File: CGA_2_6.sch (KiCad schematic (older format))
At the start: 16 parts, among them U10 74153, U101 74S174, U24 74LS244, U31 74S08, U32 74LS166, U33 MK36000, U34 74LS273, U35 74LS273, U36 74LS244, U37 74LS374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

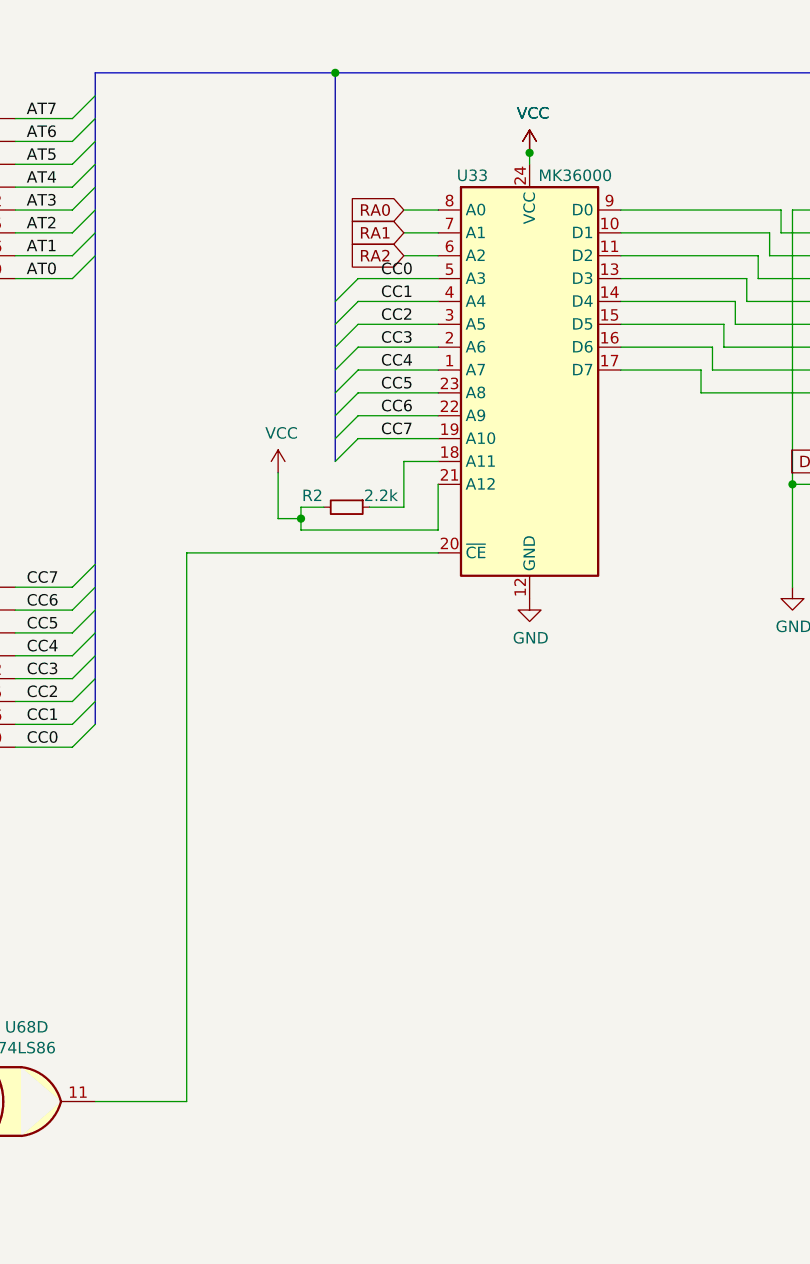
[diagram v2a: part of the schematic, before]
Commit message: Replace MK36000 with 27C256
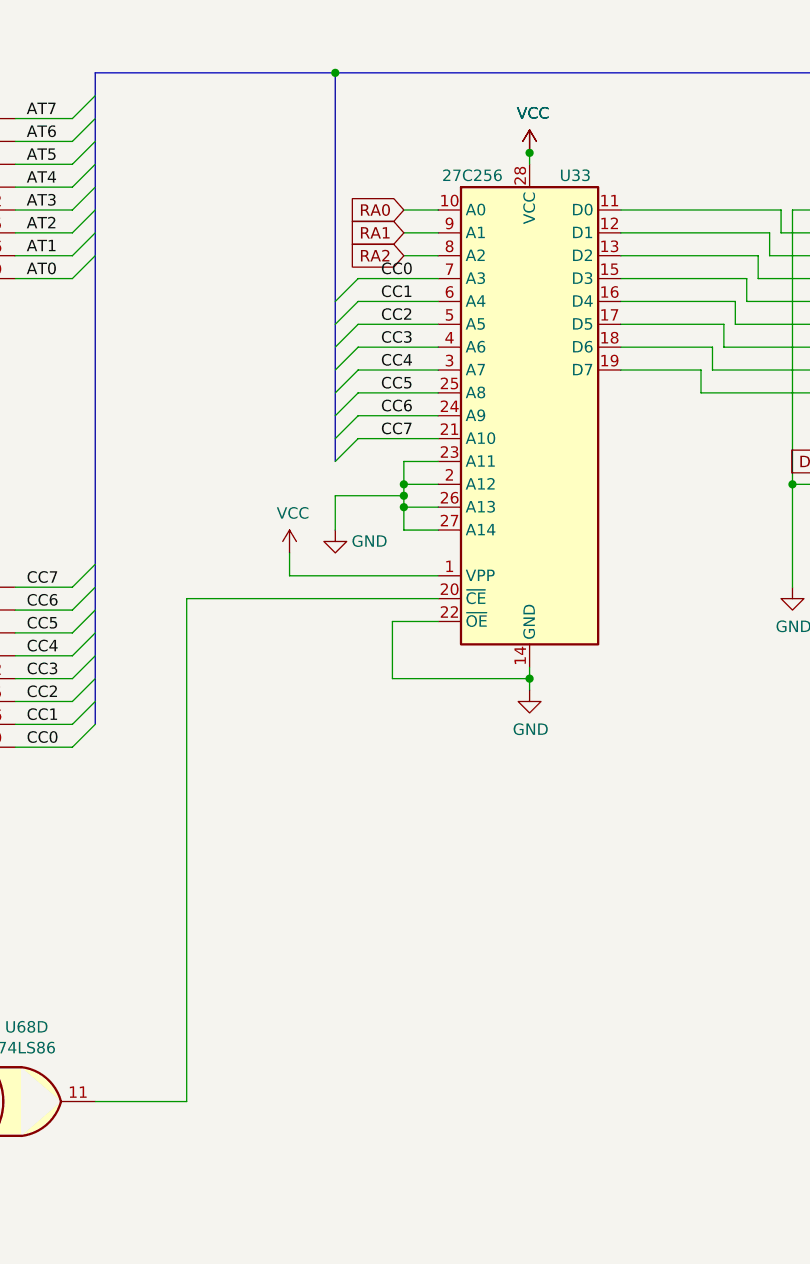
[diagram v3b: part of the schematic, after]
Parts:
- removed R2: 2.2k, Resistor_THT:R_Axial_DIN0207_L6.3mm_D2.5mm_P10.16mm_Horizontal, symbol Device:R_Small
- removed U33: MK36000, Package_DIP:DIP-24_W15.24mm_LongPads, symbol ISA_CGA:MK36000
- added U33: 27C256, Package_DIP:DIP-28_W15.24mm_LongPads, symbol Memory_EPROM:27C256
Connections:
- net CC0: now also U33.7 (A3)
- net CC1: now also U33.6 (A4)
- net CC2: now also U33.5 (A5)
- net CC3: now also U33.4 (A6)
- net CC4: now also U33.3 (A7)
- net CC5: now also U33.25 (A8)
- net CC6: now also U33.24 (A9)
- net CC7: now also U33.21 (A10)
- net GND: now also U33.14 (GND), U33.2 (A12), U33.22 (~OE), U33.23 (A11), U33.26 (A13), U33.27 (A14)
- net RA0: now also U33.10 (A0)
- net RA1: now also U33.9 (A1)
- net RA2: now also U33.8 (A2)
- net VCC: now also U33.1 (VPP), U33.28 (VCC)
- net at U68.11: now also U33.20 (~CE)
- net at U32.10 (E): now also U33.16 (D4)
- net at U32.11 (F): now also U33.17 (D5)
- net at U32.12 (G): now also U33.18 (D6)
- net at U32.14 (H): now also U33.19 (D7)
- net at U32.2 (A): now also U33.11 (D0)
- net at U32.3 (B): now also U33.12 (D1)
- net at U32.4 (C): now also U33.13 (D2)
- net at U32.5 (D): now also U33.15 (D3)
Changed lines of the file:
@@
 Wire Wire Line
 	4800 5650 4800 5600
-Wire Wire Line
-	3300 7350 3300 9750
-Wire Wire Line
-	4400 7350 3300 7350
-Wire Wire Line
-	3800 7200 3800 7150
-Connection ~ 3800 7200
-Wire Wire Line
-	3700 7200 3800 7200
-Wire Wire Line
-	3700 7000 3700 7200
-$Comp
-L power:VCC #PWR0135
-U 1 1 61467276
-P 3700 7000
-F 0 "#PWR0135" H 3700 6850 50  0001 C CNN
-F 1 "VCC" H 3715 7173 50  0000 C CNN
-F 2 "" H 3700 7000 50  0001 C CNN
-F 3 "" H 3700 7000 50  0001 C CNN
-	1    3700 7000
-	1    0    0    -1
-$EndComp
-Wire Wire Line
-	3800 7150 3900 7150
-Wire Wire Line
-	3800 7250 3800 7200
-Wire Wire Line
-	4400 7250 3800 7250
-Wire Wire Line
-	4400 7050 4400 7250
-Wire Wire Line
-	4250 7150 4100 7150
-Wire Wire Line
-	4250 6950 4250 7150
-Wire Wire Line
-	4250 6950 4400 6950
 $Comp
 L power:VCC #PWR0136
@@
 L power:GND #PWR0137
 U 1 1 612DF480
-P 4800 7550
-F 0 "#PWR0137" H 4800 7300 50  0001 C CNN
-F 1 "GND" H 4805 7377 50  0000 C CNN
-F 2 "" H 4800 7550 50  0001 C CNN
-F 3 "" H 4800 7550 50  0001 C CNN
-	1    4800 7550
-	1    0    0    -1
-$EndComp
-$Comp
-L ISA_CGA:MK36000 U33
-U 1 1 612D802D
-P 4800 6750
-F 0 "U33" H 4550 7800 50  0000 C CNN
-F 1 "MK36000" H 5000 7800 50  0000 C CNN
-F 2 "Package_DIP:DIP-24_W15.24mm_LongPads" H 4800 6750 50  0001 C CNN
-F 3 "" H 4800 6750 50  0001 C CNN
-	1    4800 6750
-	1    0    0    -1
-$EndComp
-$Comp
-L Device:R_Small R2
-U 1 1 612D31E2
-P 4000 7150
-F 0 "R2" V 3950 7000 50  0000 C CNN
-F 1 "2.2k" V 3950 7300 50  0000 C CNN
-F 2 "Resistor_THT:R_Axial_DIN0207_L6.3mm_D2.5mm_P10.16mm_Horizontal" H 4000 7150 50  0001 C CNN
-F 3 "~" H 4000 7150 50  0001 C CNN
-	1    4000 7150
-	0    1    1    0
+P 4800 7950
+F 0 "#PWR0137" H 4800 7700 50  0001 C CNN
+F 1 "GND" H 4805 7777 50  0000 C CNN
+F 2 "" H 4800 7950 50  0001 C CNN
+F 3 "" H 4800 7950 50  0001 C CNN
+	1    4800 7950
+	1    0    0    -1
 $EndComp
 Wire Wire Line
@@
 Wire Wire Line
 	7150 5550 7150 5500
+Wire Wire Line
+	3300 9750 3300 7550
+Wire Wire Line
+	3300 7550 4400 7550
+$Comp
+L power:GND #PWR?
+U 1 1 607BFC6B
+P 3950 7250
+F 0 "#PWR?" H 3950 7000 50  0001 C CNN
+F 1 "GND" H 4100 7200 50  0000 C CNN
+F 2 "" H 3950 7250 50  0001 C CNN
+F 3 "" H 3950 7250 50  0001 C CNN
+	1    3950 7250
+	1    0    0    -1
+$EndComp
+Wire Wire Line
+	4400 7650 4200 7650
+Wire Wire Line
+	4800 7950 4800 7900
+Wire Wire Line
+	4200 7900 4800 7900
+Wire Wire Line
+	4200 7650 4200 7900
+Connection ~ 4800 7900
+Wire Wire Line
+	4800 7900 4800 7850
+$Comp
+L Memory_EPROM:27C256 U33
+U 1 1 60665940
+P 4800 6750
+F 0 "U33" H 5000 7800 50  0000 C CNN
+F 1 "27C256" H 4550 7800 50  0000 C CNN
+F 2 "Package_DIP:DIP-28_W15.24mm_LongPads" H 4800 6750 50  0001 C CNN
+F 3 "http://ww1.microchip.com/downloads/en/DeviceDoc/doc0014.pdf" H 4800 6750 50  0001 C CNN
+	1    4800 6750
+	1    0    0    -1
+$EndComp
+Wire Wire Line
+	4400 6950 4250 6950
+Wire Wire Line
+	4250 6950 4250 7050
+Wire Wire Line
+	4250 7250 4400 7250
+Wire Wire Line
+	4400 7150 4250 7150
+Connection ~ 4250 7150
+Wire Wire Line
+	4250 7150 4250 7250
+Wire Wire Line
+	4400 7050 4250 7050
+Connection ~ 4250 7050
+Wire Wire Line
+	4250 7050 4250 7100
+Wire Wire Line
+	4250 7100 3950 7100
+Wire Wire Line
+	3950 7100 3950 7250
+Connection ~ 4250 7100
+Wire Wire Line
+	4250 7100 4250 7150
+$Comp
+L power:VCC #PWR?
+U 1 1 609738F2
+P 3750 7350
+F 0 "#PWR?" H 3750 7200 50  0001 C CNN
+F 1 "VCC" H 3765 7523 50  0000 C CNN
+F 2 "" H 3750 7350 50  0001 C CNN
+F 3 "" H 3750 7350 50  0001 C CNN
+	1    3750 7350
+	1    0    0    -1
+$EndComp
+Wire Wire Line
+	4400 7450 3750 7450
+Wire Wire Line
+	3750 7450 3750 7350
 Wire Bus Line
 	5350 1200 5350 4100

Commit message: Changed footprints, moving components
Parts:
- U10, U101, U32, U39, U7, U8, U9: footprint Package_DIP:DIP-16_W7.62mm_LongPads -> Package_DIP:DIP-16_W7.62mm
- U24, U34, U35, U36, U37: footprint Package_DIP:DIP-20_W7.62mm_LongPads -> Package_DIP:DIP-20_W7.62mm
- U31, U68: footprint Package_DIP:DIP-14_W7.62mm_LongPads -> Package_DIP:DIP-14_W7.62mm
- U33: footprint Package_DIP:DIP-28_W15.24mm_LongPads -> Package_DIP:DIP-28_W15.24mm
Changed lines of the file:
@@
 F 0 "U101" H 14250 7000 50  0000 C CNN
 F 1 "74S174" H 14700 7000 50  0000 C CNN
-F 2 "Package_DIP:DIP-16_W7.62mm_LongPads" H 14500 6450 50  0001 C CNN
+F 2 "Package_DIP:DIP-16_W7.62mm" H 14500 6450 50  0001 C CNN
 F 3 "http://www.ti.com/lit/gpn/sn74LS174" H 14500 6450 50  0001 C CNN
 	1    14500 6450
@@
 F 0 "U31" H 8600 8925 50  0000 C CNN
 F 1 "74S08" H 8600 8834 50  0000 C CNN
-F 2 "Package_DIP:DIP-14_W7.62mm_LongPads" H 8600 8600 50  0001 C CNN
+F 2 "Package_DIP:DIP-14_W7.62mm" H 8600 8600 50  0001 C CNN
 F 3 "http://www.ti.com/lit/gpn/sn74LS08" H 8600 8600 50  0001 C CNN
 	3    8600 8600
@@
 F 0 "U10" H 11200 10200 50  0000 C CNN
 F 1 "74153" H 11650 10200 50  0000 C CNN
-F 2 "Package_DIP:DIP-16_W7.62mm_LongPads" H 11450 9350 50  0001 C CNN
+F 2 "Package_DIP:DIP-16_W7.62mm" H 11450 9350 50  0001 C CNN
 F 3 "http://www.ti.com/lit/gpn/sn74LS153" H 11450 9350 50  0001 C CNN
 	1    11450 9350
@@
 F 0 "U9" H 11200 7600 50  0000 C CNN
 F 1 "74153" H 11650 7600 50  0000 C CNN
-F 2 "Package_DIP:DIP-16_W7.62mm_LongPads" H 11450 6750 50  0001 C CNN
+F 2 "Package_DIP:DIP-16_W7.62mm" H 11450 6750 50  0001 C CNN
 F 3 "http://www.ti.com/lit/gpn/sn74LS153" H 11450 6750 50  0001 C CNN
 	1    11450 6750
@@
 F 0 "U8" H 11150 5100 50  0000 L CNN
 F 1 "74LS166" H 11500 5100 50  0000 L CNN
-F 2 "Package_DIP:DIP-16_W7.62mm_LongPads" H 11450 4250 50  0001 C CNN
+F 2 "Package_DIP:DIP-16_W7.62mm" H 11450 4250 50  0001 C CNN
 F 3 "http://www.ti.com/lit/gpn/sn74LS166" H 11450 4250 50  0001 C CNN
 	1    11450 4250
@@
 F 0 "U7" H 11150 2600 50  0000 L CNN
 F 1 "74LS166" H 11500 2600 50  0000 L CNN
-F 2 "Package_DIP:DIP-16_W7.62mm_LongPads" H 11450 1750 50  0001 C CNN
+F 2 "Package_DIP:DIP-16_W7.62mm" H 11450 1750 50  0001 C CNN
 F 3 "http://www.ti.com/lit/gpn/sn74LS166" H 11450 1750 50  0001 C CNN
 	1    11450 1750
@@
 F 0 "U32" H 6850 7400 50  0000 L CNN
 F 1 "74LS166" H 7200 7400 50  0000 L CNN
-F 2 "Package_DIP:DIP-16_W7.62mm_LongPads" H 7150 6550 50  0001 C CNN
+F 2 "Package_DIP:DIP-16_W7.62mm" H 7150 6550 50  0001 C CNN
 F 3 "http://www.ti.com/lit/gpn/sn74LS166" H 7150 6550 50  0001 C CNN
 	1    7150 6550
@@
 F 0 "U68" H 2600 10075 50  0000 C CNN
 F 1 "74LS86" H 2600 9984 50  0000 C CNN
-F 2 "Package_DIP:DIP-14_W7.62mm_LongPads" H 2600 9750 50  0001 C CNN
+F 2 "Package_DIP:DIP-14_W7.62mm" H 2600 9750 50  0001 C CNN
 F 3 "74xx/74ls86.pdf" H 2600 9750 50  0001 C CNN
 	4    2600 9750
@@
 F 0 "U68" H 1700 9975 50  0000 C CNN
 F 1 "74LS86" H 1700 9884 50  0000 C CNN
-F 2 "Package_DIP:DIP-14_W7.62mm_LongPads" H 1700 9650 50  0001 C CNN
+F 2 "Package_DIP:DIP-14_W7.62mm" H 1700 9650 50  0001 C CNN
 F 3 "74xx/74ls86.pdf" H 1700 9650 50  0001 C CNN
 	3    1700 9650
@@
 F 0 "U39" H 6700 2700 50  0000 C CNN
 F 1 "74LS174" H 7150 2700 50  0000 C CNN
-F 2 "Package_DIP:DIP-16_W7.62mm_LongPads" H 6950 2150 50  0001 C CNN
+F 2 "Package_DIP:DIP-16_W7.62mm" H 6950 2150 50  0001 C CNN
 F 3 "http://www.ti.com/lit/gpn/sn74LS174" H 6950 2150 50  0001 C CNN
 	1    6950 2150
@@
 F 0 "U34" H 1800 8650 50  0000 C CNN
 F 1 "74LS273" H 2250 8650 50  0000 C CNN
-F 2 "Package_DIP:DIP-20_W7.62mm_LongPads" H 2050 8000 50  0001 C CNN
+F 2 "Package_DIP:DIP-20_W7.62mm" H 2050 8000 50  0001 C CNN
 F 3 "http://www.ti.com/lit/gpn/sn74LS273" H 2050 8000 50  0001 C CNN
 	1    2050 8000
@@
 F 0 "U35" H 1800 6600 50  0000 C CNN
 F 1 "74LS273" H 2250 6600 50  0000 C CNN
-F 2 "Package_DIP:DIP-20_W7.62mm_LongPads" H 2050 5950 50  0001 C CNN
+F 2 "Package_DIP:DIP-20_W7.62mm" H 2050 5950 50  0001 C CNN
 F 3 "http://www.ti.com/lit/gpn/sn74LS273" H 2050 5950 50  0001 C CNN
 	1    2050 5950
@@
 F 0 "U37" H 1800 4550 50  0000 C CNN
 F 1 "74LS374" H 2250 4550 50  0000 C CNN
-F 2 "Package_DIP:DIP-20_W7.62mm_LongPads" H 2050 3900 50  0001 C CNN
+F 2 "Package_DIP:DIP-20_W7.62mm" H 2050 3900 50  0001 C CNN
 F 3 "http://www.ti.com/lit/gpn/sn74LS374" H 2050 3900 50  0001 C CNN
 	1    2050 3900
@@
 F 0 "U36" H 1800 2500 50  0000 C CNN
 F 1 "74LS244" H 2250 2500 50  0000 C CNN
-F 2 "Package_DIP:DIP-20_W7.62mm_LongPads" H 2050 1850 50  0001 C CNN
+F 2 "Package_DIP:DIP-20_W7.62mm" H 2050 1850 50  0001 C CNN
 F 3 "http://www.ti.com/lit/ds/symlink/sn74ls244.pdf" H 2050 1850 50  0001 C CNN
 	1    2050 1850
@@
 F 0 "U24" H 4450 2800 50  0000 C CNN
 F 1 "74LS244" H 5000 2800 50  0000 C CNN
-F 2 "Package_DIP:DIP-20_W7.62mm_LongPads" H 4750 2900 50  0001 C CNN
+F 2 "Package_DIP:DIP-20_W7.62mm" H 4750 2900 50  0001 C CNN
 F 3 "http://www.ti.com/lit/ds/symlink/sn74ls241.pdf" H 4750 2900 50  0001 C CNN
 	5    4750 2900
@@
 F 0 "U24" H 4450 2450 50  0000 C CNN
 F 1 "74LS244" H 5000 2450 50  0000 C CNN
-F 2 "Package_DIP:DIP-20_W7.62mm_LongPads" H 4750 2550 50  0001 C CNN
+F 2 "Package_DIP:DIP-20_W7.62mm" H 4750 2550 50  0001 C CNN
 F 3 "http://www.ti.com/lit/ds/symlink/sn74ls241.pdf" H 4750 2550 50  0001 C CNN
 	6    4750 2550
@@
 F 0 "U24" H 4450 2100 50  0000 C CNN
 F 1 "74LS244" H 5000 2100 50  0000 C CNN
-F 2 "Package_DIP:DIP-20_W7.62mm_LongPads" H 4750 2200 50  0001 C CNN
+F 2 "Package_DIP:DIP-20_W7.62mm" H 4750 2200 50  0001 C CNN
 F 3 "http://www.ti.com/lit/ds/symlink/sn74ls241.pdf" H 4750 2200 50  0001 C CNN
 	7    4750 2200
@@
 F 0 "U24" H 4450 1750 50  0000 C CNN
 F 1 "74LS244" H 5000 1750 50  0000 C CNN
-F 2 "Package_DIP:DIP-20_W7.62mm_LongPads" H 4750 1850 50  0001 C CNN
+F 2 "Package_DIP:DIP-20_W7.62mm" H 4750 1850 50  0001 C CNN
 F 3 "http://www.ti.com/lit/ds/symlink/sn74ls241.pdf" H 4750 1850 50  0001 C CNN
 	8    4750 1850
@@
 F 0 "U33" H 5000 7800 50  0000 C CNN
 F 1 "27C256" H 4550 7800 50  0000 C CNN
-F 2 "Package_DIP:DIP-28_W15.24mm_LongPads" H 4800 6750 50  0001 C CNN
+F 2 "Package_DIP:DIP-28_W15.24mm" H 4800 6750 50  0001 C CNN
 F 3 "http://ww1.microchip.com/downloads/en/DeviceDoc/doc0014.pdf" H 4800 6750 50  0001 C CNN
 	1    4800 6750

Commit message: Rewire 27C256 so a dump from the original MK36000 can be used unchanged
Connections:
- net GND: no longer U33.2 (A12), U33.23 (A11)
- net VCC: now also U33.2 (A12), U33.23 (A11)
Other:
- note added: "The original board uses an MK36000 ROM chip\nto keep characters.\n\nThis type of ROM has address lines A0-A12, where\nA11 and A12 are tied HIGH.\n\nMK36000 is 64k-bit or 8K-byte."
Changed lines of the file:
@@
 $EndComp
-Wire Wire Line
-	4400 6950 4250 6950
-Wire Wire Line
-	4250 6950 4250 7050
 Wire Wire Line
 	4250 7250 4400 7250
 Wire Wire Line
 	4400 7150 4250 7150
-Connection ~ 4250 7150
 Wire Wire Line
-	4250 7150 4250 7250
-Wire Wire Line
-	4400 7050 4250 7050
-Connection ~ 4250 7050
-Wire Wire Line
-	4250 7050 4250 7100
-Wire Wire Line
-	4250 7100 3950 7100
-Wire Wire Line
-	3950 7100 3950 7250
-Connection ~ 4250 7100
-Wire Wire Line
-	4250 7100 4250 7150
+	4250 7150 4250 7200
 $Comp
 L power:VCC #PWR0155
@@
 Wire Wire Line
 	3750 7450 3750 7350
+Text Notes 4050 8700 0    39   ~ 0
+The original board uses an MK36000 ROM chip\nto keep characters.\n\nThis type of ROM has address lines A0-A12, where\nA11 and A12 are tied HIGH.\n\nMK36000 is 64k-bit or 8K-byte.
+Wire Wire Line
+	4250 7200 3950 7200
+Wire Wire Line
+	3950 7200 3950 7250
+Connection ~ 4250 7200
+Wire Wire Line
+	4250 7200 4250 7250
+Wire Wire Line
+	4400 7050 4300 7050
+Wire Wire Line
+	4300 7050 4300 7000
+Wire Wire Line
+	4300 6950 4400 6950
+Wire Wire Line
+	4300 7000 3750 7000
+Wire Wire Line
+	3750 7000 3750 6900
 Wire Bus Line
 	5350 1200 5350 4100
@@
 Wire Bus Line
 	1250 1450 1250 8300
+Connection ~ 4300 7000
+Wire Wire Line
+	4300 7000 4300 6950
+$Comp
+L power:VCC #PWR?
+U 1 1 609B869D
+P 3750 6900
+F 0 "#PWR?" H 3750 6750 50  0001 C CNN
+F 1 "VCC" H 3765 7073 50  0000 C CNN
+F 2 "" H 3750 6900 50  0001 C CNN
+F 3 "" H 3750 6900 50  0001 C CNN
+	1    3750 6900
+	1    0    0    -1
+$EndComp
 $EndSCHEMATC
